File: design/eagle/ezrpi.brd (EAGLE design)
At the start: 100 x 80 mm, 27 parts

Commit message: completed schematic, started work on board design
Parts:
- added C0, CR2: 1uF, passive:0805
- added CM, CM3: 2.7pF, passive:0805
- added CM2: 5.1pF, passive:0805
- added CR1: 3pF, passive:0805
- added L0: 19nH, passive:C0402
- added LCHOKE: 120nH, passive:0805
- added LM, LM2: 9.1nH, passive:0805
- added LR1: 20nH, passive:0805
- added LR2: 24nH, passive:0805
- added X1: (no value), connector:SMA90_DIP
- R1: value 1 -> 1 Ω
- moved U$3 122.7 mm to (66.0, 73.7)
- moved U$5 86.0 mm to (38.1, 73.7)
- moved U$2 81.3 mm to (2.54, 2.54)
- moved U$4 78.5 mm to (48.3, 73.7)
- moved U$6 71.4 mm to (34.3, 67.3)
- moved U$1 60.1 mm to (29.5, 29.4), turned to 180 degrees
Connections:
- removed net GND-ISO: C1.2, C10.2, C11.2, C12.2, C13.2, C14.2, C15.2, C16.2, C17.2, C18.2, C19.2, C2.2, C3.2, C4.2, C5.2, C6.2, C7.2, C8.2, C9.2, U$1.65, U$2.14, U$2.20, U$2.25, U$2.30, U$2.34, U$2.39, U$2.6, U$2.9, U$3.5, U$4.2, U$4.4, U$5.2, U$5.4
- new net GND: C1.2, C10.2, C11.2, C12.2, C13.2, C14.2, C15.2, C16.2, C17.2, C18.2, C19.2, C2.2, C3.2, C4.2, C5.2, C6.2, C7.2, C8.2, C9.2, CM.2, CM2.2, CM3.2, CR1.2, U$1.65, U$2.14, U$2.20, U$2.25, U$2.30, U$2.34, U$2.39, U$2.6, U$2.9, U$3.5, U$4.2, U$4.4, U$5.2, U$5.4, X1.GND1, X1.GND2, X1.GND3, X1.GND4
- new net N$1: CM3.1, LM2.2, X1.ANTENNA
- new net N$3: CM2.1, LM.2, LM2.1
- new net N$5: U$2.8
- new net N$6: C0.2, L0.1
- new net N$7: CM.1, CR2.2, L0.2, LM.1, LR2.2
- new net N$8: U$2.10
- net RXN: now also CR2.1, LR1.1
- net RXP: now also CR1.1, LR1.2, LR2.1
- net TX_13: now also C0.1, LCHOKE.2
- net VCC: now also LCHOKE.1
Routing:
- added copper zone on layer 16, net GND
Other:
- board size 100 x 80 mm -> 65 x 56 mm

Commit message: completed schematic and first board layout
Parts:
- moved C6 121.8 mm to (42.1, 36.5), turned to 90 degrees
- moved C5 120.9 mm to (45.0, 36.5), turned to 90 degrees
- moved C19 110.1 mm to (44.0, 40.3), turned to 90 degrees
- moved L1 102.7 mm to (31.0, 47.5), turned to 270 degrees
- moved C18 102.3 mm to (39.5, 40.3), turned to 90 degrees
- moved C4 97.8 mm to (25.3, 37.4)
- moved R1 96.5 mm to (28.1, 47.4), turned to 270 degrees
- moved C3 93.4 mm to (25.3, 40.2)
- moved C17 91.1 mm to (32.7, 43.7), turned to 90 degrees
- moved C16 90.3 mm to (35.6, 43.7), turned to 90 degrees
- moved C2 89.1 mm to (25.4, 43.2)
- moved C1 84.9 mm to (25.4, 46.0)
- moved C15 82.7 mm to (28.6, 37.3), turned to 180 degrees
- moved C14 79.9 mm to (33.6, 47.5), turned to 90 degrees
- moved C13 79.0 mm to (36.4, 47.5), turned to 90 degrees
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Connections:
- removed net N$5: U$2.8
- removed net N$8: U$2.10
- new net RX: U$1.43, U$2.8
- new net TX: U$1.42, U$2.10
- net LFXN: now also C18.1, U$6.1; no longer C19.1, U$6.2
- net LFXP: now also C19.1, U$6.2; no longer C18.1, U$6.1
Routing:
- net VCC: track 0.00 -> 109.5 mm
- net GND: track 0.00 -> 108.4 mm, vias 0 -> 10
- net IOVDD: track 0.00 -> 47.8 mm, vias 0 -> 3
- net RESET: track 0.00 -> 46.0 mm, vias 0 -> 2
- net RX: track 0.00 -> 32.1 mm, vias 0 -> 1
- net AVDD: track 0.00 -> 30.1 mm
- net TX: track 0.00 -> 29.3 mm, vias 0 -> 1
- net RXP: track 0.00 -> 9.63 mm
- net N$7: track 0.00 -> 8.94 mm
- net SWO: track 0.00 -> 8.55 mm
- net XIN: track 0.00 -> 7.84 mm
- net RXN: track 0.00 -> 7.76 mm
- net N$1: track 0.00 -> 7.48 mm
- net SWCLK: track 0.00 -> 7.48 mm, vias 0 -> 2
- net TX_13: track 0.00 -> 6.64 mm
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
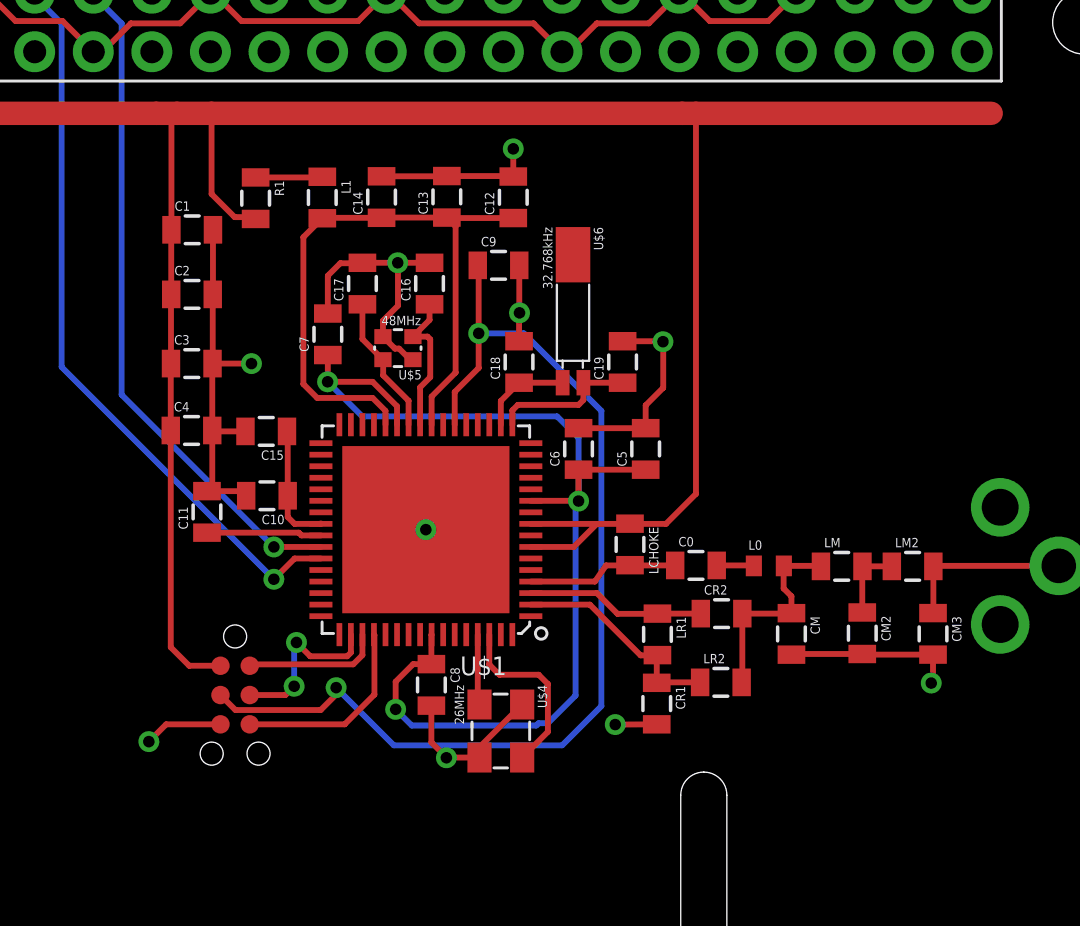
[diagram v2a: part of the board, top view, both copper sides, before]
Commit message: fixed some design rules violations
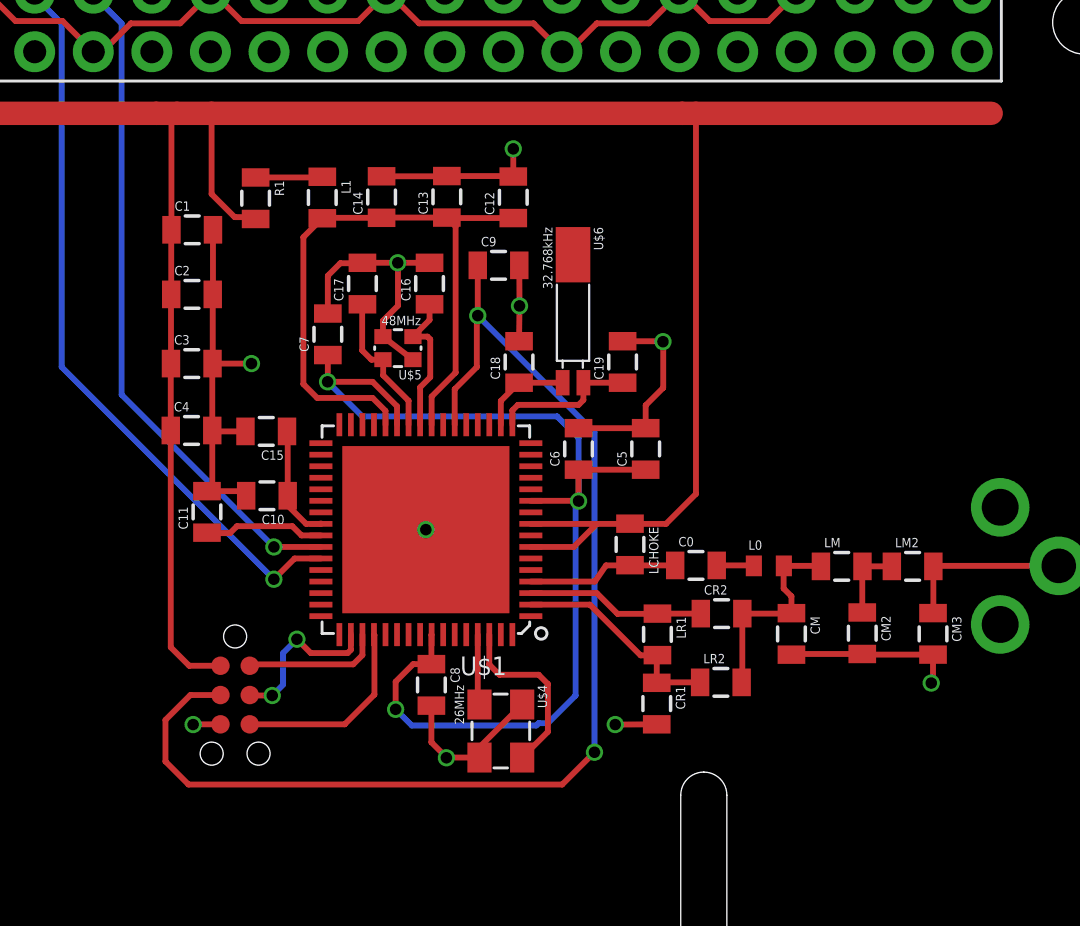
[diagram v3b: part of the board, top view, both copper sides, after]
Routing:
- net RESET: track 46.0 -> 52.6 mm
- net GND: track 108.4 -> 106.1 mm

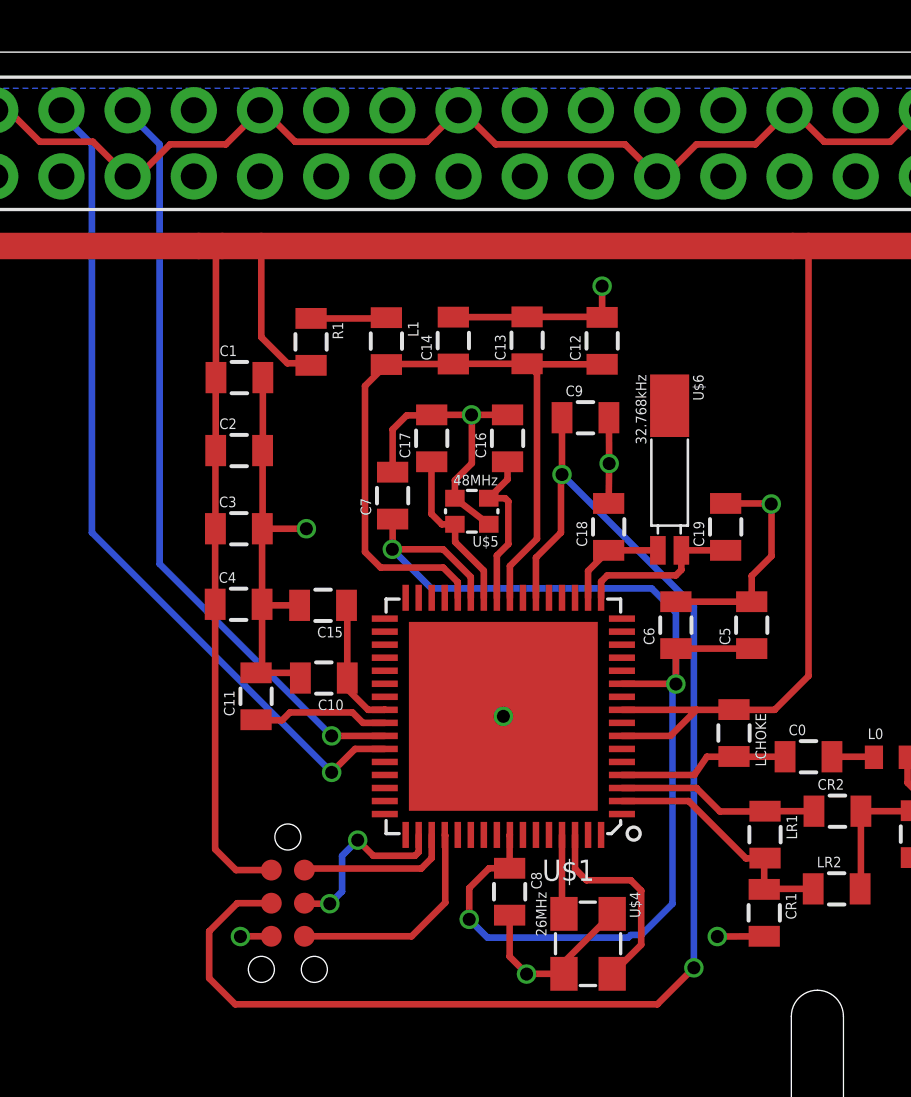
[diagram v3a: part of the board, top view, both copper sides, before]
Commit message: fixed incorrect pin connection on IOVDD_0
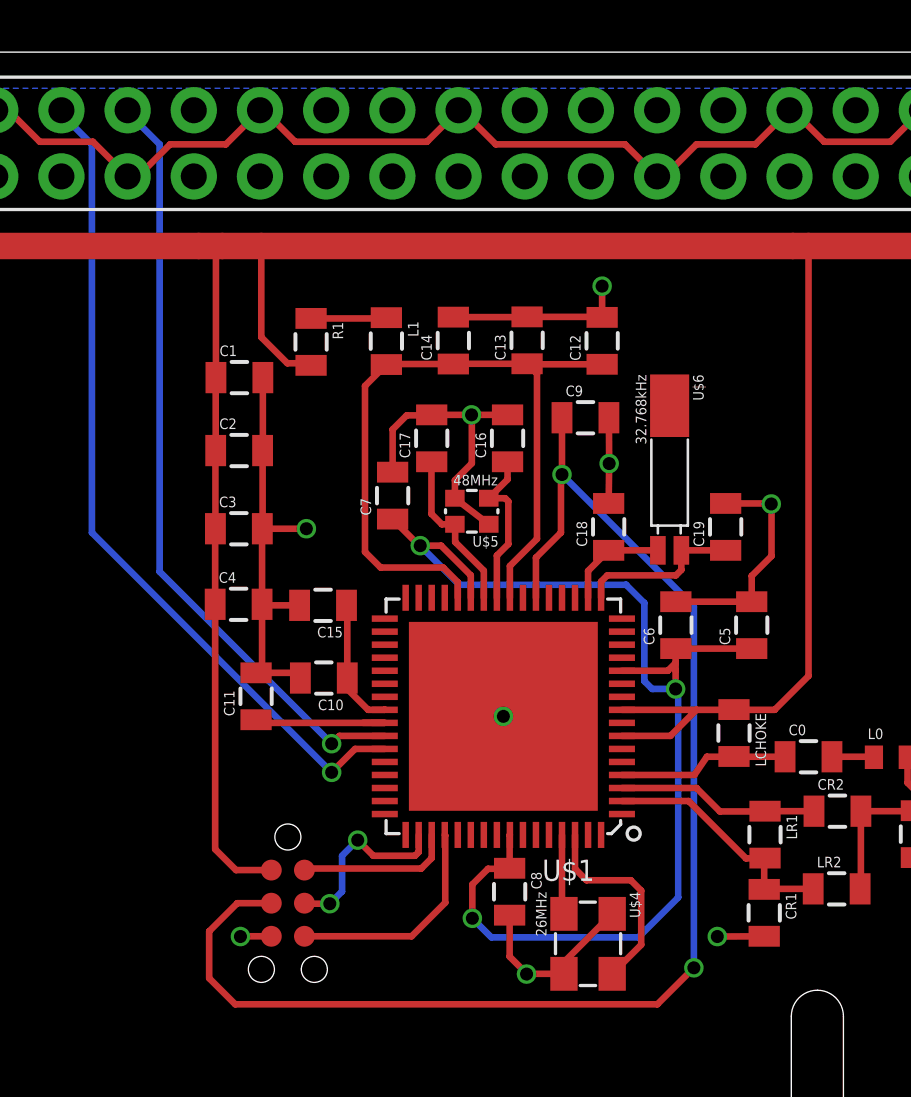
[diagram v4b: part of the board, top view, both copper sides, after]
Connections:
- net IOVDD: now also U$1.12; no longer U$1.11
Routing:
- net IOVDD: track 47.8 -> 46.4 mm
- net N$2: track 5.24 -> 5.86 mm
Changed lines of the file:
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@@
 </signal>
 <signal name="IOVDD">
-<contactref element="U$1" pad="11"/>
 <contactref element="C6" pad="1"/>
 <contactref element="C7" pad="1"/>
@@
 <contactref element="C8" pad="1"/>
 <contactref element="C5" pad="1"/>
-<wire x1="35.73" y1="28.49" x2="35.73" y2="27.22" width="0.254" layer="1"/>
+<wire x1="35.73" y1="27.22" x2="35.73" y2="28.49" width="0.254" layer="1"/>
 <wire x1="35.73" y1="28.49" x2="35.74" y2="28.5" width="0.254" layer="1"/>
-<wire x1="34.24" y1="37.6" x2="34.24" y2="38.4" width="0.254" layer="1"/>
-<wire x1="34.24" y1="38.4" x2="33.18" y2="39.46" width="0.254" layer="1"/>
-<wire x1="31.23" y1="39.46" x2="33.18" y2="39.46" width="0.254" layer="1"/>
-<via x="31.23" y="39.46" extent="1-16" drill="0.5" diameter="0.254"/>
-<wire x1="31.24" y1="40.62" x2="31.24" y2="39.47" width="0.254" layer="1"/>
-<wire x1="31.24" y1="39.47" x2="31.23" y2="39.46" width="0.254" layer="1"/>
-<wire x1="42.11" y1="34.3" x2="40.04" y2="34.3" width="0.254" layer="1"/>
-<wire x1="42.11" y1="34.3" x2="42.11" y2="34.29" width="0.254" layer="1"/>
-<via x="42.11" y="34.29" extent="1-16" drill="0.5" diameter="0.254"/>
-<wire x1="42.11" y1="34.29" x2="42.11" y2="37.03" width="0.254" layer="16"/>
-<wire x1="42.11" y1="37.03" x2="41.18" y2="37.96" width="0.254" layer="16"/>
-<wire x1="41.18" y1="37.96" x2="32.73" y2="37.96" width="0.254" layer="16"/>
-<wire x1="32.73" y1="37.96" x2="31.23" y2="39.46" width="0.254" layer="16"/>
-<wire x1="42.11" y1="34.3" x2="42.11" y2="35.65" width="0.254" layer="1"/>
-<wire x1="42.11" y1="35.65" x2="45.02" y2="35.65" width="0.254" layer="1"/>
-<wire x1="35.73" y1="27.22" x2="34.94" y2="27.22" width="0.254" layer="1"/>
-<wire x1="34.94" y1="27.22" x2="34.18" y2="26.46" width="0.254" layer="1"/>
-<wire x1="34.18" y1="26.46" x2="34.18" y2="25.26" width="0.254" layer="1"/>
-<via x="34.18" y="25.26" extent="1-16" drill="0.5"/>
-<wire x1="34.18" y1="25.26" x2="34.88" y2="24.56" width="0.254" layer="16"/>
-<wire x1="34.88" y1="24.56" x2="40.28" y2="24.56" width="0.254" layer="16"/>
-<wire x1="40.28" y1="24.56" x2="40.38" y2="24.66" width="0.254" layer="16"/>
-<wire x1="40.38" y1="24.66" x2="40.78" y2="24.66" width="0.254" layer="16"/>
-<wire x1="40.78" y1="24.66" x2="41.98" y2="25.86" width="0.254" layer="16"/>
-<wire x1="41.98" y1="25.86" x2="41.98" y2="34.16" width="0.254" layer="16"/>
-<wire x1="41.98" y1="34.16" x2="42.11" y2="34.29" width="0.254" layer="16"/>
+<wire x1="45.02" y1="35.65" x2="42.11" y2="35.65" width="0.254" layer="1"/>
+<contactref element="U$1" pad="12"/>
+<wire x1="42.11" y1="35.65" x2="42.1" y2="35.64" width="0.254" layer="1"/>
+<wire x1="42.1" y1="35.1" x2="42.1" y2="35.64" width="0.254" layer="1"/>
+<wire x1="42.1" y1="35.1" x2="42.1" y2="34.8" width="0.254" layer="1"/>
+<wire x1="42.1" y1="34.8" x2="42.1" y2="34.1" width="0.254" layer="1"/>
+<via x="42.1" y="34.1" extent="1-16" drill="0.5"/>
+<wire x1="42.2" y1="34" x2="42.1" y2="34.1" width="0.254" layer="16"/>
+<wire x1="42.2" y1="34" x2="42.2" y2="26.1" width="0.254" layer="16"/>
+<wire x1="42.2" y1="26.1" x2="40.67" y2="24.57" width="0.254" layer="16"/>
+<wire x1="40.67" y1="24.57" x2="35.03" y2="24.57" width="0.254" layer="16"/>
+<wire x1="35.03" y1="24.57" x2="34.3" y2="25.3" width="0.254" layer="16"/>
+<via x="34.3" y="25.3" extent="1-16" drill="0.5"/>
+<wire x1="34.3" y1="25.3" x2="34.3" y2="26.6" width="0.254" layer="1"/>
+<wire x1="34.3" y1="26.6" x2="34.9" y2="27.2" width="0.254" layer="1"/>
+<wire x1="34.9" y1="27.2" x2="35.71" y2="27.2" width="0.254" layer="1"/>
+<wire x1="35.71" y1="27.2" x2="35.73" y2="27.22" width="0.254" layer="1"/>
+<wire x1="40.04" y1="34.8" x2="41.8" y2="34.8" width="0.254" layer="1"/>
+<wire x1="41.8" y1="34.8" x2="42.1" y2="35.1" width="0.254" layer="1"/>
+<wire x1="42.1" y1="34.1" x2="41.2" y2="34.1" width="0.254" layer="16"/>
+<wire x1="41.2" y1="34.1" x2="40.9" y2="34.4" width="0.254" layer="16"/>
+<wire x1="40.9" y1="34.4" x2="40.9" y2="37.4" width="0.254" layer="16"/>
+<wire x1="40.9" y1="37.4" x2="40.2" y2="38.1" width="0.254" layer="16"/>
+<wire x1="40.2" y1="38.1" x2="33.8" y2="38.1" width="0.254" layer="16"/>
+<wire x1="33.8" y1="38.1" x2="32.3" y2="39.6" width="0.254" layer="16"/>
+<via x="32.3" y="39.6" extent="1-16" drill="0.5"/>
+<wire x1="32.3" y1="39.6" x2="32.26" y2="39.6" width="0.254" layer="1"/>
+<wire x1="32.26" y1="39.6" x2="31.24" y2="40.62" width="0.254" layer="1"/>
+<wire x1="34.24" y1="37.6" x2="34.24" y2="38.46" width="0.254" layer="1"/>
+<wire x1="34.24" y1="38.46" x2="33.1" y2="39.6" width="0.254" layer="1"/>
+<wire x1="33.1" y1="39.6" x2="32.3" y2="39.6" width="0.254" layer="1"/>
 </signal>
 <signal name="N$4">
@@
 <contactref element="U$1" pad="41"/>
 <contactref element="C11" pad="1"/>
-<wire x1="30.94" y1="32.8" x2="30.1" y2="32.8" width="0.254" layer="1"/>
-<wire x1="30.1" y1="32.8" x2="29.7" y2="33.2" width="0.254" layer="1"/>
-<wire x1="29.7" y1="33.2" x2="27.3" y2="33.2" width="0.254" layer="1"/>
-<wire x1="27.3" y1="33.2" x2="27" y2="32.9" width="0.254" layer="1"/>
-<wire x1="27" y1="32.9" x2="26.02" y2="32.9" width="0.254" layer="1"/>
-<wire x1="26.02" y1="32.9" x2="26" y2="32.92" width="0.254" layer="1"/>
+<wire x1="30.1" y1="32.8" x2="30.94" y2="32.8" width="0.254" layer="1"/>
+<wire x1="26" y1="32.92" x2="26.02" y2="32.9" width="0.254" layer="1"/>
+<wire x1="30.94" y1="32.8" x2="26.12" y2="32.8" width="0.254" layer="1"/>
+<wire x1="26.12" y1="32.8" x2="26" y2="32.92" width="0.254" layer="1"/>
 </signal>
 <signal name="VDD">
@@
 <wire x1="21.07" y1="56.31" x2="21.07" y2="56.23" width="0.254" layer="16"/>
 <wire x1="21.07" y1="56.23" x2="22.3" y2="55" width="0.254" layer="16"/>
-<wire x1="22.3" y1="55" x2="22.3" y2="38.9" width="0.254" layer="16"/>
-<wire x1="22.3" y1="38.9" x2="28.9" y2="32.3" width="0.254" layer="16"/>
-<via x="28.9" y="32.3" extent="1-16" drill="0.5"/>
-<wire x1="28.9" y1="32.3" x2="30.94" y2="32.3" width="0.254" layer="1"/>
+<wire x1="22.3" y1="55" x2="22.3" y2="38.6" width="0.254" layer="16"/>
+<wire x1="22.3" y1="38.6" x2="28.9" y2="32" width="0.254" layer="16"/>
+<via x="28.9" y="32" extent="1-16" drill="0.5"/>
+<wire x1="28.9" y1="32" x2="29.2" y2="32.3" width="0.254" layer="1"/>
+<wire x1="29.2" y1="32.3" x2="30.94" y2="32.3" width="0.254" layer="1"/>
 </signal>
 </signals>

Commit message: unified cap value 100nF = 0.1uF
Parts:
- C9: value 100nF -> 0.1uF
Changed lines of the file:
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@@
 <element name="C7" library="passive" package="0805" value="0.1uF" x="31.24" y="41.52" rot="R90"/>
 <element name="C8" library="passive" package="0805" value="0.1uF" x="35.73" y="26.32" rot="R270"/>
-<element name="C9" library="passive" package="0805" value="100nF" x="38.64" y="44.51"/>
+<element name="C9" library="passive" package="0805" value="0.1uF" x="38.64" y="44.51"/>
 <element name="L1" library="passive" package="0805" value="1 kΩ" x="31" y="47.45" rot="R270"/>
 <element name="R1" library="passive" package="0805" value="1 Ω" x="28.11" y="47.42" rot="R270"/>
